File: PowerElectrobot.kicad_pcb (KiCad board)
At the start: 2 copper layers, 87.4 x 68.1 mm, 80 parts, among them J10 Conn_XT30F, J11 Conn_XT30F, J12 Conn_XT30F, J13 Conn_XT30F, J14 Conn_XT30F, J15 Conn_XT30F, J16 Conn_XT30F, J17 Conn_XT30F, J18 Conn_XT30F, J19 Conn_XT30F, J2 Conn_XT60M, J3 Conn_XT30F, J4 Conn_XT30F, J5 Conn_XT30F, J6 Conn_XT30F, J7 Conn_XT30F, J8 Conn_01x04, J9 Conn_01x04, Q1 BTS117, Q2 BTS117, Q3 BTS117, Q4 BTS117, Q5 BTS117, Q6 BTS117, Q7 BTS117, Q8 BTS117, U1 DSPIC33FJ128MC802-xSP, U2 TSR_2-2450, U3 MCP1804x-3302xDB, U4 ACS712xLCTR-05B, U5 ACS712xLCTR-05B, U6 ACS712xLCTR-20A

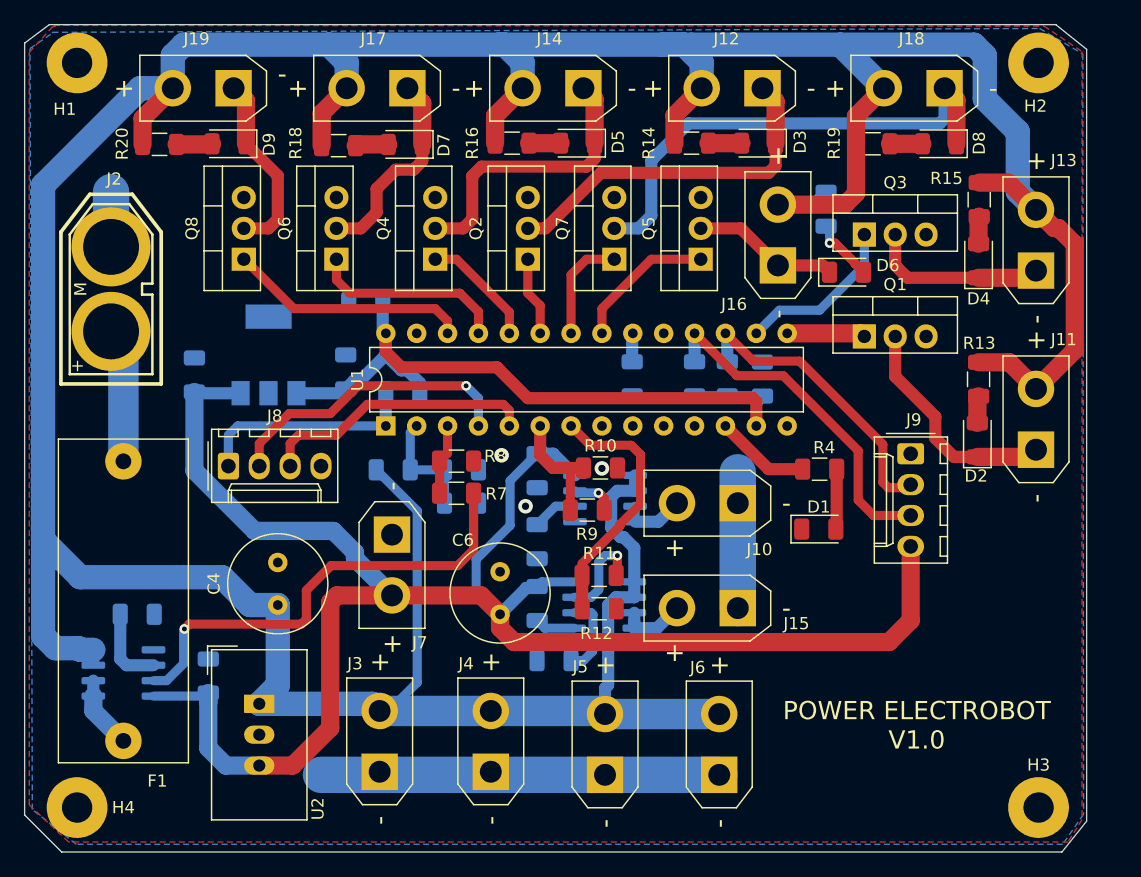
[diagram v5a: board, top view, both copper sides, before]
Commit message: Ajout sérigraphie et dimensions
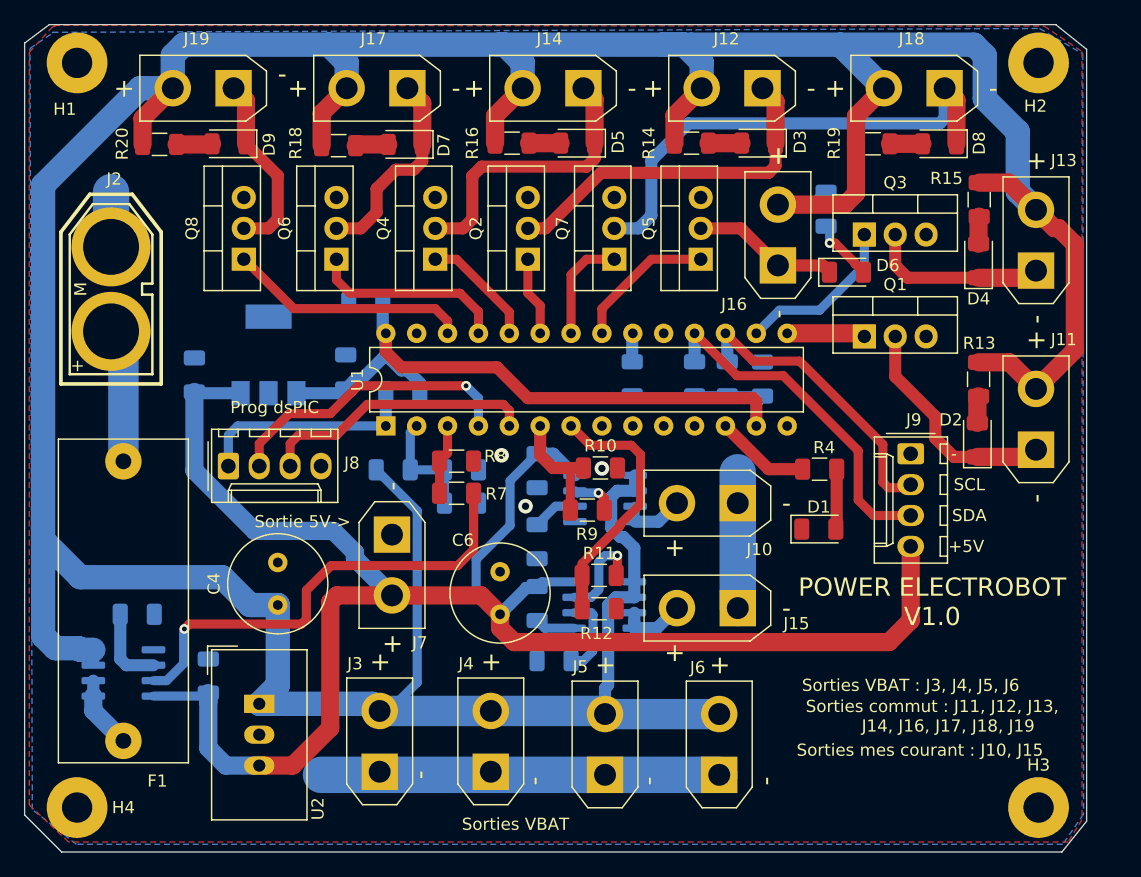
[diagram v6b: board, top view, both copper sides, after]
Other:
- board text added: "+5V"
- board text added: "-"
- board text added: "Prog dsPIC"
- board text added: "SCL"
- board text added: "SDA"
- board text added: "Sortie 5V->"
- board text added: "Sorties VBAT"
- board text added: "Sorties VBAT : J3, J4, J5, J6"
- board text added: "Sorties commut : J11, J12, J13, J14, J16, J17, J18, J19"
- board text added: "Sorties mes courant : J10, J15"
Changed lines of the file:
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@@
   (general
     (thickness 1.6)
-    (drawings 9)
+    (drawings 24)
     (tracks 383)
     (zones 0)
@@
   )
   (setup
-    (last_trace_width 3)
+    (last_trace_width 0.25)
     (user_trace_width 0.5)
     (user_trace_width 0.75)
@@
       (effects (font (size 1 1) (thickness 0.15)))
     )
-    (fp_text user - (at -4 0 90) (layer F.SilkS)
+    (fp_text user - (at -0.254 3.302 90) (layer F.SilkS)
       (effects (font (size 1.5 1.5) (thickness 0.15)))
     )
@@
       (effects (font (size 1.5 1.5) (thickness 0.15)))
     )
-    (fp_text user - (at -4 0 90) (layer F.SilkS)
+    (fp_text user - (at -0.762 3.556 90) (layer F.SilkS)
       (effects (font (size 1.5 1.5) (thickness 0.15)))
     )
@@
       (effects (font (size 1.5 1.5) (thickness 0.15)))
     )
-    (fp_text user - (at -4 0 90) (layer F.SilkS)
+    (fp_text user - (at -0.508 3.556 90) (layer F.SilkS)
       (effects (font (size 1.5 1.5) (thickness 0.15)))
     )
@@
       (effects (font (size 1 1) (thickness 0.15)))
     )
-    (fp_text user - (at -4 0 90) (layer F.SilkS)
+    (fp_text user - (at -0.508 3.81 90) (layer F.SilkS)
       (effects (font (size 1.5 1.5) (thickness 0.15)))
     )
@@
     (descr "Molex KK-254 Interconnect System, old/engineering part number: AE-6410-04A example for new part number: 22-27-2041, 4 Pins (http://www.molex.com/pdm_docs/sd/022272021_sd.pdf), generated with kicad-footprint-generator")
     (tags "connector Molex KK-254 side entry")
-    (fp_text reference J8 (at 3.81 -4.12) (layer F.SilkS)
+    (fp_text reference J8 (at 10.16 -0.254) (layer F.SilkS)
       (effects (font (size 1 1) (thickness 0.15)))
     )
@@
     (tags diode)
     (attr smd)
-    (fp_text reference D2 (at -2.9688 -0.1016) (layer F.SilkS)
+    (fp_text reference D2 (at 1.654 -2.1844) (layer F.SilkS)
       (effects (font (size 1 1) (thickness 0.15)))
     )
@@
     )
   )
+  (gr_circle (center 72.39 111.125) (end 72.59 111.125) (layer B.SilkS) (width 0.5))
+  (gr_circle (center 120.523 101.6) (end 120.723 101.6) (layer B.SilkS) (width 0.5))
+  (gr_circle (center 120.65 92.964) (end 120.85 92.964) (layer B.SilkS) (width 0.5))
+  (gr_text - (at 145.034 91.186) (layer F.SilkS)
+    (effects (font (size 1 1) (thickness 0.15)))
+  )
+  (gr_text SDA (at 146.304 96.266) (layer F.SilkS)
+    (effects (font (size 1 1) (thickness 0.15)))
+  )
+  (gr_text SCL (at 146.304 93.726) (layer F.SilkS)
+    (effects (font (size 1 1) (thickness 0.15)))
+  )
+  (gr_text +5V (at 146.05 98.806) (layer F.SilkS)
+    (effects (font (size 1 1) (thickness 0.15)))
+  )
+  (gr_text "Sorties mes courant : J10, J15" (at 142.24 115.57) (layer F.SilkS)
+    (effects (font (size 1 1) (thickness 0.15)))
+  )
+  (gr_text "Sorties commut : J11, J12, J13, \n      J14, J16, J17, J18, J19" (at 143.256 112.776) (layer F.SilkS)
+    (effects (font (size 1 1) (thickness 0.15)))
+  )
+  (gr_text "Sorties VBAT" (at 108.966 121.666) (layer F.SilkS)
+    (effects (font (size 1 1) (thickness 0.15)))
+  )
+  (gr_text "Prog dsPIC" (at 89.154 87.376) (layer F.SilkS)
+    (effects (font (size 1 1) (thickness 0.15)))
+  )
+  (gr_text "Sorties VBAT : J3, J4, J5, J6" (at 141.478 110.236) (layer F.SilkS)
+    (effects (font (size 1 1) (thickness 0.15)))
+  )
+  (gr_text "Sortie 5V->" (at 91.44 96.774) (layer F.SilkS)
+    (effects (font (size 1 1) (thickness 0.15)))
+  )
+  (dimension 61.2648 (width 0.12) (layer Dwgs.User)
+    (gr_text "61,265 mm" (at 163.83 89.662 270) (layer Dwgs.User)
+      (effects (font (size 1 1) (thickness 0.15)))
+    )
+    (feature1 (pts (xy 152 120.2944) (xy 163.146421 120.2944)))
+    (feature2 (pts (xy 152 59.0296) (xy 163.146421 59.0296)))
+    (crossbar (pts (xy 162.56 59.0296) (xy 162.56 120.2944)))
+    (arrow1a (pts (xy 162.56 120.2944) (xy 161.973579 119.167896)))
+    (arrow1b (pts (xy 162.56 120.2944) (xy 163.146421 119.167896)))
+    (arrow2a (pts (xy 162.56 59.0296) (xy 161.973579 60.156104)))
+    (arrow2b (pts (xy 162.56 59.0296) (xy 163.146421 60.156104)))
+  )
+  (dimension 79.102004 (width 0.12) (layer Dwgs.User)
+    (gr_text "79,102 mm" (at 112.445539 131.059204) (layer Dwgs.User)
+      (effects (font (size 1 1) (thickness 0.15)))
+    )
+    (feature1 (pts (xy 152 120.2944) (xy 151.996759 130.388324)))
+    (feature2 (pts (xy 72.898 120.269) (xy 72.894759 130.362924)))
+    (crossbar (pts (xy 72.894947 129.776504) (xy 151.996947 129.801904)))
+    (arrow1a (pts (xy 151.996947 129.801904) (xy 150.870255 130.387963)))
+    (arrow1b (pts (xy 151.996947 129.801904) (xy 150.870632 129.215122)))
+    (arrow2a (pts (xy 72.894947 129.776504) (xy 74.021262 130.363286)))
+    (arrow2b (pts (xy 72.894947 129.776504) (xy 74.021639 129.190445)))
+  )
   (gr_line (start 68.58 57.404) (end 70.612 55.88) (layer Edge.Cuts) (width 0.05))
   (gr_line (start 68.58 120.904) (end 68.58 57.404) (layer Edge.Cuts) (width 0.05))
@@
   (gr_line (start 153.416 55.88) (end 155.956 57.912) (layer Edge.Cuts) (width 0.05))
   (gr_line (start 70.612 55.88) (end 153.416 55.88) (layer Edge.Cuts) (width 0.05))
-  (gr_text "POWER ELECTROBOT\nV1.0" (at 141.986 113.538) (layer F.SilkS)
+  (gr_text "POWER ELECTROBOT\nV1.0" (at 143.256 103.378) (layer F.SilkS)
     (effects (font (size 1.5 1.5) (thickness 0.15)))
   )
